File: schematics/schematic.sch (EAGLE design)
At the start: 14 parts, among them U1 TSR_1-2450

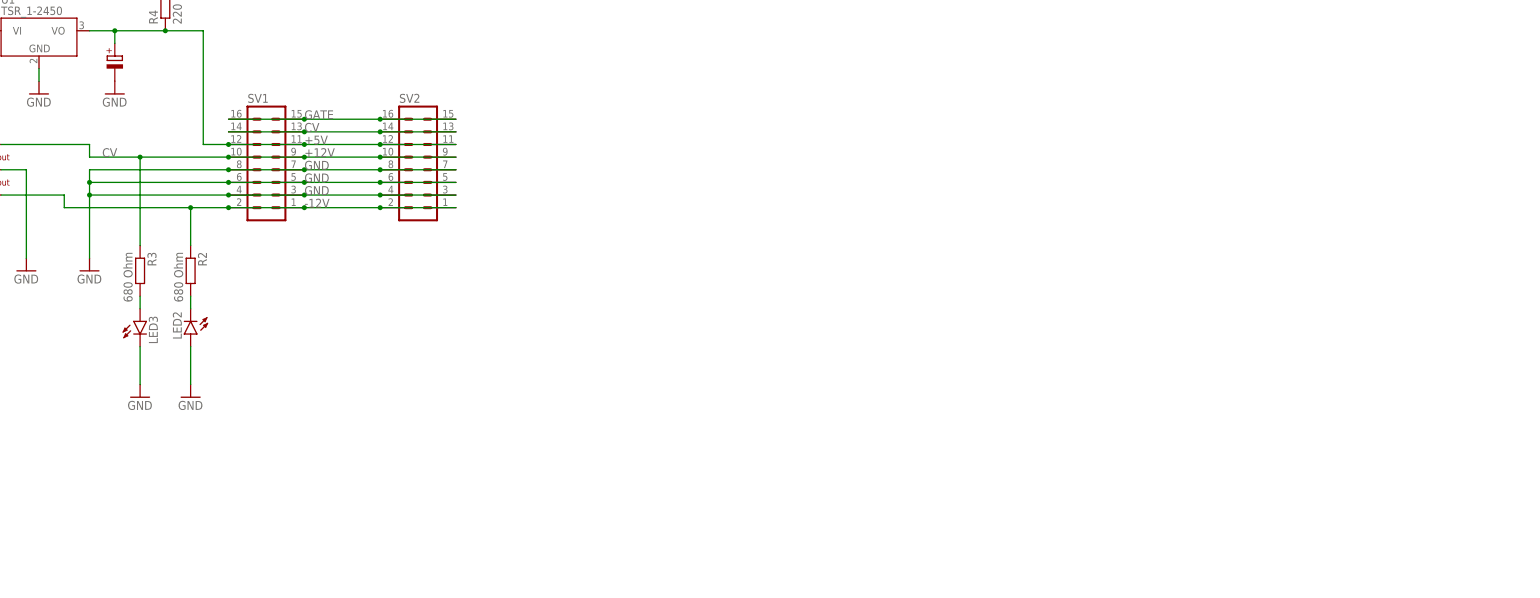
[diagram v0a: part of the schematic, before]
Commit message: changed schematic
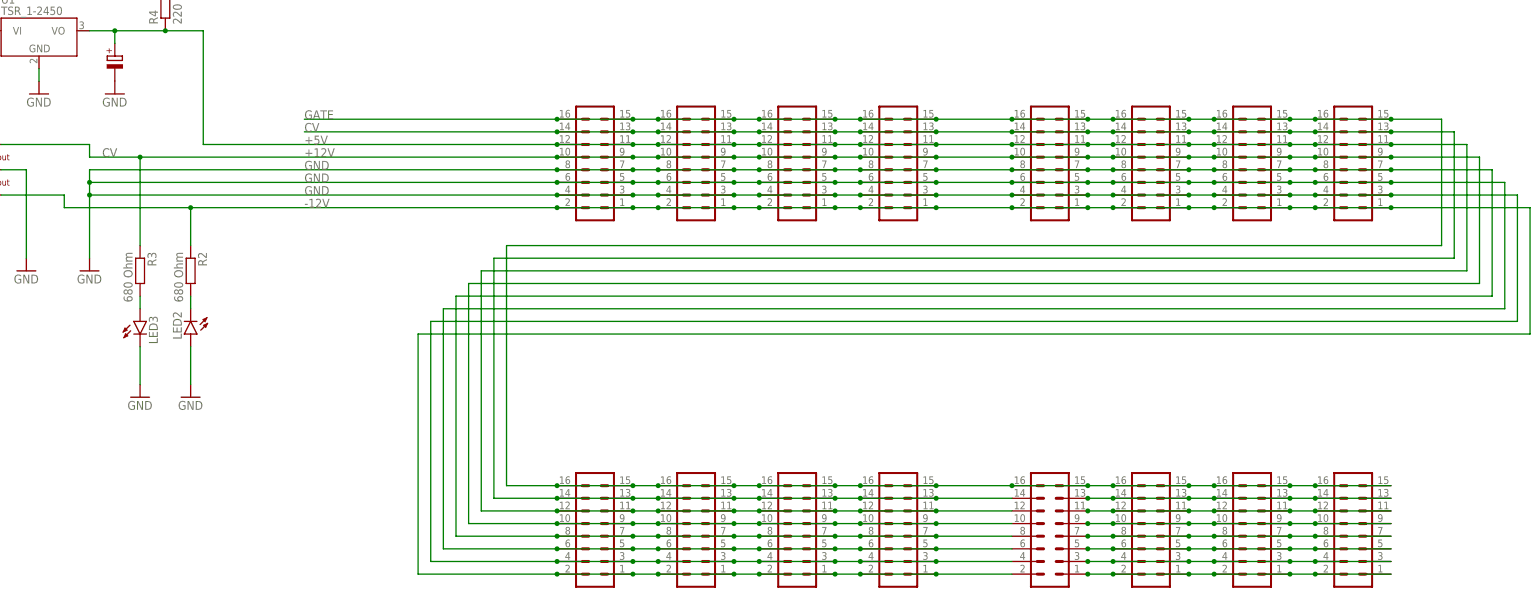
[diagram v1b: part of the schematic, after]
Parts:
- removed SV1: (no value), con-lstb:MA08-2W
- added SV10, SV11, SV12, SV13, SV14, SV15, SV16, SV17, SV3, SV4, SV5, SV6, SV7, SV8, SV9: (no value), con-lstb:MA08-2W
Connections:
- new net N$30: SV14.1, SV15.1, SV15.2, SV16.1, SV16.2, SV17.1, SV17.2
- new net N$31: SV14.3, SV15.3, SV15.4, SV16.3, SV16.4, SV17.3, SV17.4
- new net N$32: SV14.5, SV15.5, SV15.6, SV16.5, SV16.6, SV17.5, SV17.6
- new net N$33: SV14.7, SV15.7, SV15.8, SV16.7, SV16.8, SV17.7, SV17.8
- new net N$34: SV14.9, SV15.10, SV15.9, SV16.10, SV16.9, SV17.10, SV17.9
- new net N$35: SV14.11, SV15.11, SV15.12, SV16.11, SV16.12, SV17.11, SV17.12
- new net N$36: SV14.13, SV15.13, SV15.14, SV16.13, SV16.14, SV17.13, SV17.14
- net +12V: now also SV10.10, SV10.9, SV11.10, SV11.9, SV12.10, SV12.9, SV13.10, SV13.9, SV14.10, SV3.10, SV3.9, SV4.10, SV4.9, SV5.10, SV5.9, SV6.10, SV6.9, SV7.10, SV7.9, SV8.10, SV8.9, SV9.10, SV9.9; no longer SV1.10, SV1.9
- net +5V: now also SV10.11, SV10.12, SV11.11, SV11.12, SV12.11, SV12.12, SV13.11, SV13.12, SV14.12, SV3.11, SV3.12, SV4.11, SV4.12, SV5.11, SV5.12, SV6.11, SV6.12, SV7.11, SV7.12, SV8.11, SV8.12, SV9.11, SV9.12; no longer SV1.11, SV1.12
- net -12V: now also SV10.1, SV10.2, SV11.1, SV11.2, SV12.1, SV12.2, SV13.1, SV13.2, SV14.2, SV3.1, SV3.2, SV4.1, SV4.2, SV5.1, SV5.2, SV6.1, SV6.2, SV7.1, SV7.2, SV8.1, SV8.2, SV9.1, SV9.2; no longer SV1.1, SV1.2
- net CV: now also SV10.13, SV10.14, SV11.13, SV11.14, SV12.13, SV12.14, SV13.13, SV13.14, SV14.14, SV3.13, SV3.14, SV4.13, SV4.14, SV5.13, SV5.14, SV6.13, SV6.14, SV7.13, SV7.14, SV8.13, SV8.14, SV9.13, SV9.14; no longer SV1.13, SV1.14
- net GATE: now also SV10.15, SV10.16, SV11.15, SV11.16, SV12.15, SV12.16, SV13.15, SV13.16, SV14.15, SV14.16, SV15.15, SV15.16, SV16.15, SV16.16, SV17.15, SV17.16, SV3.15, SV3.16, SV4.15, SV4.16, SV5.15, SV5.16, SV6.15, SV6.16, SV7.15, SV7.16, SV8.15, SV8.16, SV9.15, SV9.16; no longer SV1.15, SV1.16
- net GND: now also SV10.3, SV10.4, SV10.5, SV10.6, SV10.7, SV10.8, SV11.3, SV11.4, SV11.5, SV11.6, SV11.7, SV11.8, SV12.3, SV12.4, SV12.5, SV12.6, SV12.7, SV12.8, SV13.3, SV13.4, SV13.5, SV13.6, SV13.7, SV13.8, SV14.4, SV14.6, SV14.8, SV3.3, SV3.4, SV3.5, SV3.6, SV3.7, SV3.8, SV4.3, SV4.4, SV4.5, SV4.6, SV4.7, SV4.8, SV5.3, SV5.4, SV5.5, SV5.6, SV5.7, SV5.8, SV6.3, SV6.4, SV6.5, SV6.6, SV6.7, SV6.8, SV7.3, SV7.4, SV7.5, SV7.6, SV7.7, SV7.8, SV8.3, SV8.4, SV8.5, SV8.6, SV8.7, SV8.8, SV9.3, SV9.4, SV9.5, SV9.6, SV9.7, SV9.8; no longer SV1.3, SV1.4, SV1.5, SV1.6, SV1.7, SV1.8

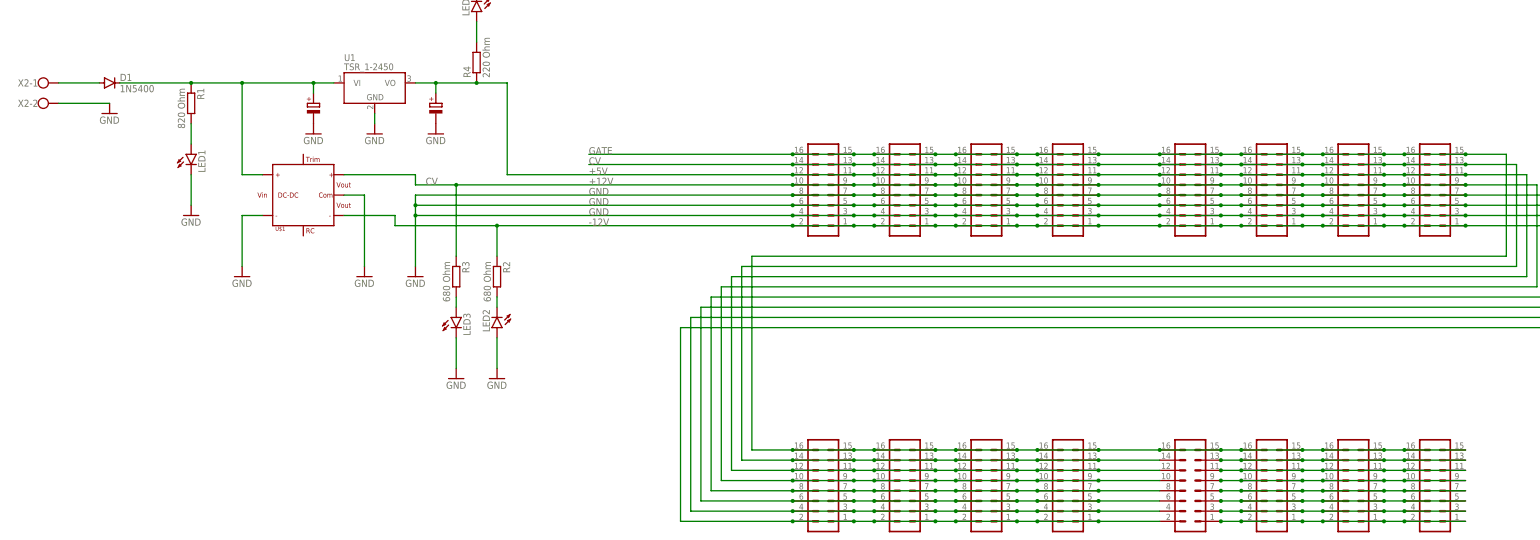
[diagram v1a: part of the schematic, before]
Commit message: fixed power header connections
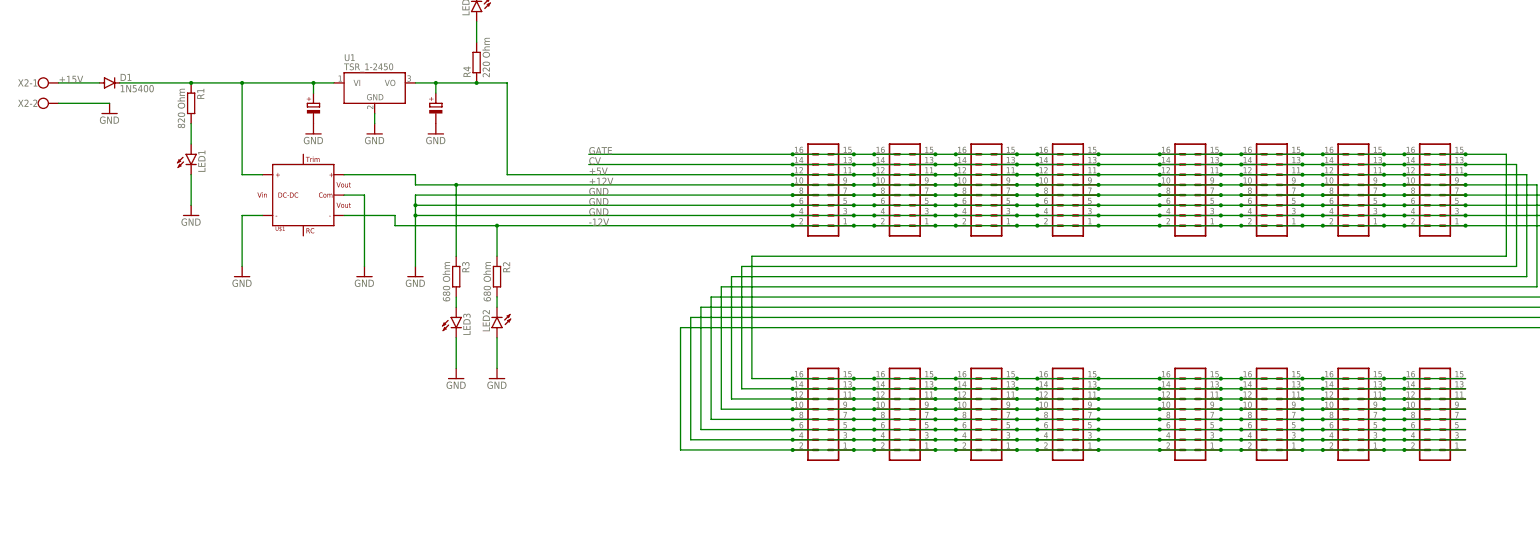
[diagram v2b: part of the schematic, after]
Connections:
- net N$1 renamed +15V
- removed net N$30: SV14.1, SV15.1, SV15.2, SV16.1, SV16.2, SV17.1, SV17.2
- removed net N$31: SV14.3, SV15.3, SV15.4, SV16.3, SV16.4, SV17.3, SV17.4
- removed net N$32: SV14.5, SV15.5, SV15.6, SV16.5, SV16.6, SV17.5, SV17.6
- removed net N$33: SV14.7, SV15.7, SV15.8, SV16.7, SV16.8, SV17.7, SV17.8
- removed net N$34: SV14.9, SV15.10, SV15.9, SV16.10, SV16.9, SV17.10, SV17.9
- removed net N$35: SV14.11, SV15.11, SV15.12, SV16.11, SV16.12, SV17.11, SV17.12
- removed net N$36: SV14.13, SV15.13, SV15.14, SV16.13, SV16.14, SV17.13, SV17.14
- net +12V: now also SV14.9, SV15.10, SV15.9, SV16.10, SV16.9, SV17.10, SV17.9
- net +5V: now also SV14.11, SV15.11, SV15.12, SV16.11, SV16.12, SV17.11, SV17.12
- net -12V: now also SV14.1, SV15.1, SV15.2, SV16.1, SV16.2, SV17.1, SV17.2
- net CV: now also SV14.13, SV15.13, SV15.14, SV16.13, SV16.14, SV17.13, SV17.14
- net GND: now also SV14.3, SV14.5, SV14.7, SV15.3, SV15.4, SV15.5, SV15.6, SV15.7, SV15.8, SV16.3, SV16.4, SV16.5, SV16.6, SV16.7, SV16.8, SV17.3, SV17.4, SV17.5, SV17.6, SV17.7, SV17.8

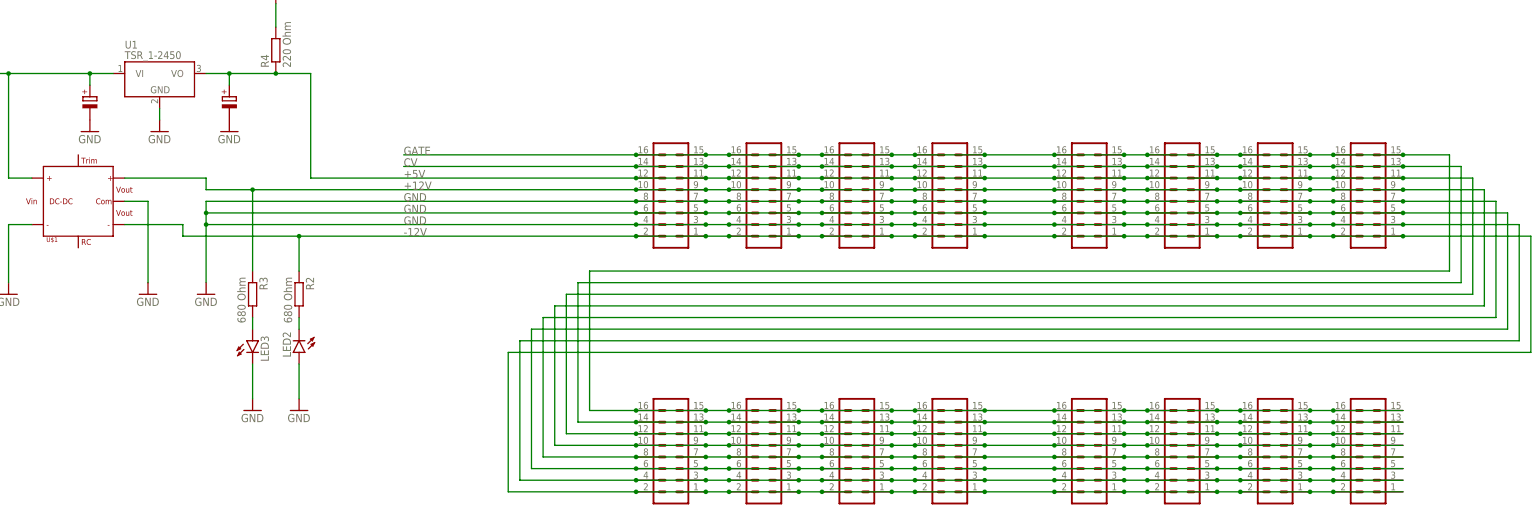
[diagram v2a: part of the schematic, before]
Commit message: added first board layout
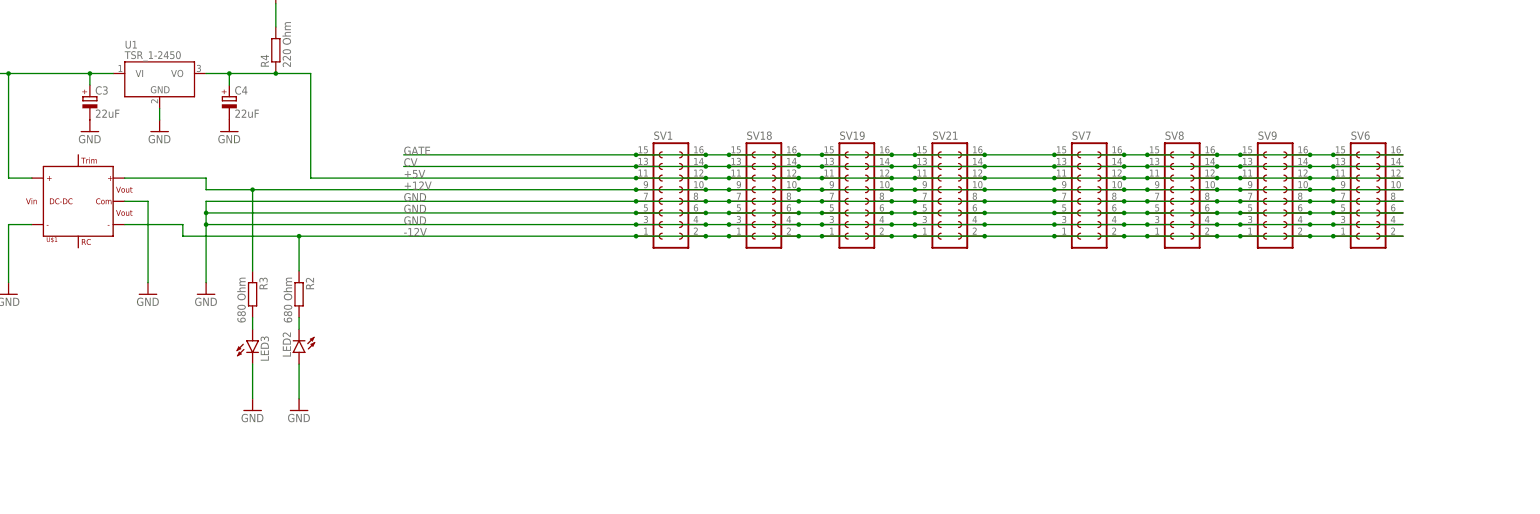
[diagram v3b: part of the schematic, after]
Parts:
- removed SV10, SV11, SV12, SV13, SV14, SV15, SV16, SV17, SV2, SV3, SV4, SV5: (no value), con-lstb:MA08-2W
- added C3, C4: 22uF, rcl:CPOL-EUE2.5-5
- added SV1, SV18, SV19, SV21: (no value), con-lsta:FE08-2
- R1, R2, R3, R4: device rcl:R-EU_0204/7 -> rcl:R-EU_0207/10
- SV6, SV7, SV8, SV9: device con-lstb:MA08-2W -> con-lsta:FE08-2
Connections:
- net +12V: now also SV1.10, SV1.9, SV18.10, SV18.9, SV19.10, SV19.9, SV21.10, SV21.9; no longer SV10.10, SV10.9, SV11.10, SV11.9, SV12.10, SV12.9, SV13.10, SV13.9, SV14.10, SV14.9, SV15.10, SV15.9, SV16.10, SV16.9, SV17.10, SV17.9, SV2.10, SV2.9, SV3.10, SV3.9, SV4.10, SV4.9, SV5.10, SV5.9
- net +5V: now also C4.+, SV1.11, SV1.12, SV18.11, SV18.12, SV19.11, SV19.12, SV21.11, SV21.12; no longer SV10.11, SV10.12, SV11.11, SV11.12, SV12.11, SV12.12, SV13.11, SV13.12, SV14.11, SV14.12, SV15.11, SV15.12, SV16.11, SV16.12, SV17.11, SV17.12, SV2.11, SV2.12, SV3.11, SV3.12, SV4.11, SV4.12, SV5.11, SV5.12
- net -12V: now also SV1.1, SV1.2, SV18.1, SV18.2, SV19.1, SV19.2, SV21.1, SV21.2; no longer SV10.1, SV10.2, SV11.1, SV11.2, SV12.1, SV12.2, SV13.1, SV13.2, SV14.1, SV14.2, SV15.1, SV15.2, SV16.1, SV16.2, SV17.1, SV17.2, SV2.1, SV2.2, SV3.1, SV3.2, SV4.1, SV4.2, SV5.1, SV5.2
- net CV: now also SV1.13, SV1.14, SV18.13, SV18.14, SV19.13, SV19.14, SV21.13, SV21.14; no longer SV10.13, SV10.14, SV11.13, SV11.14, SV12.13, SV12.14, SV13.13, SV13.14, SV14.13, SV14.14, SV15.13, SV15.14, SV16.13, SV16.14, SV17.13, SV17.14, SV2.13, SV2.14, SV3.13, SV3.14, SV4.13, SV4.14, SV5.13, SV5.14
- net GATE: now also SV1.15, SV1.16, SV18.15, SV18.16, SV19.15, SV19.16, SV21.15, SV21.16; no longer SV10.15, SV10.16, SV11.15, SV11.16, SV12.15, SV12.16, SV13.15, SV13.16, SV14.15, SV14.16, SV15.15, SV15.16, SV16.15, SV16.16, SV17.15, SV17.16, SV2.15, SV2.16, SV3.15, SV3.16, SV4.15, SV4.16, SV5.15, SV5.16
- net GND: now also C3.-, C4.-, SV1.3, SV1.4, SV1.5, SV1.6, SV1.7, SV1.8, SV18.3, SV18.4, SV18.5, SV18.6, SV18.7, SV18.8, SV19.3, SV19.4, SV19.5, SV19.6, SV19.7, SV19.8, SV21.3, SV21.4, SV21.5, SV21.6, SV21.7, SV21.8; no longer SV10.3, SV10.4, SV10.5, SV10.6, SV10.7, SV10.8, SV11.3, SV11.4, SV11.5, SV11.6, SV11.7, SV11.8, SV12.3, SV12.4, SV12.5, SV12.6, SV12.7, SV12.8, SV13.3, SV13.4, SV13.5, SV13.6, SV13.7, SV13.8, SV14.3, SV14.4, SV14.5, SV14.6, SV14.7, SV14.8, SV15.3, SV15.4, SV15.5, SV15.6, SV15.7, SV15.8, SV16.3, SV16.4, SV16.5, SV16.6, SV16.7, SV16.8, SV17.3, SV17.4, SV17.5, SV17.6, SV17.7, SV17.8, SV2.3, SV2.4, SV2.5, SV2.6, SV2.7, SV2.8, SV3.3, SV3.4, SV3.5, SV3.6, SV3.7, SV3.8, SV4.3, SV4.4, SV4.5, SV4.6, SV4.7, SV4.8, SV5.3, SV5.4, SV5.5, SV5.6, SV5.7, SV5.8
- net VI: now also C3.+

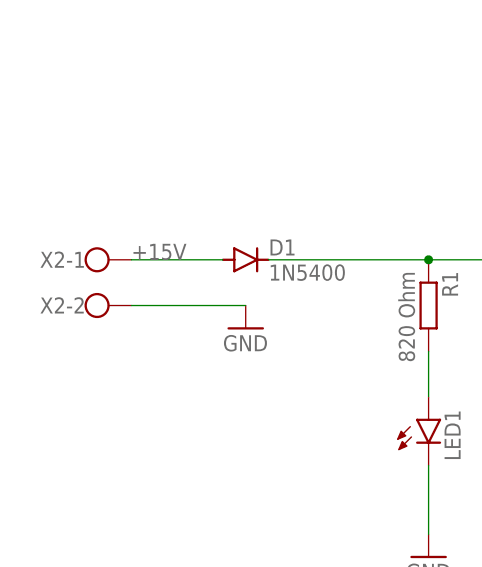
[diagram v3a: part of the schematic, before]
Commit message: added double input screw terminals
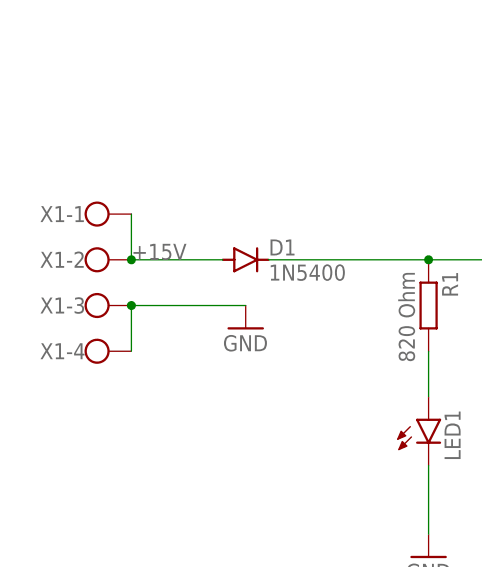
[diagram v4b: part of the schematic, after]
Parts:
- removed X2: (no value), con-wago-500:W237-102
- added X1: (no value), con-wago-500:W237-4
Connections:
- net +15V: now also X1-1.KL, X1-2.KL; no longer X2-1.KL
- net GND: now also X1-3.KL, X1-4.KL; no longer X2-2.KL
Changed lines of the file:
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@@
 <parts>
 <part name="U$1" library="dk30a" deviceset="DKA30" device="&quot;"/>
-<part name="X2" library="con-wago-500" library_urn="urn:adsk.eagle:library:195" deviceset="W237-102" device="" package3d_urn="urn:adsk.eagle:package:10688/1"/>
 <part name="GND1" library="supply1" library_urn="urn:adsk.eagle:library:371" deviceset="GND" device=""/>
 <part name="D1" library="diode" library_urn="urn:adsk.eagle:library:210" deviceset="1N5400" device="" package3d_urn="urn:adsk.eagle:package:43365/2"/>
@@
 <part name="SV8" library="con-lsta" library_urn="urn:adsk.eagle:library:161" deviceset="FE08-2" device="" package3d_urn="urn:adsk.eagle:package:8174/1"/>
 <part name="SV9" library="con-lsta" library_urn="urn:adsk.eagle:library:161" deviceset="FE08-2" device="" package3d_urn="urn:adsk.eagle:package:8174/1"/>
+<part name="X1" library="con-wago-500" library_urn="urn:adsk.eagle:library:195" deviceset="W237-4" device="" package3d_urn="urn:adsk.eagle:package:10695/1"/>
 </parts>
 <sheets>
@@
 <attribute name="NAME" x="59.055" y="59.69" size="1.016" layer="94" font="vector"/>
 </instance>
-<instance part="X2" gate="-1" x="0" y="96.52" smashed="yes">
-<attribute name="NAME" x="0" y="97.409" size="1.778" layer="95" rot="R180"/>
-</instance>
-<instance part="X2" gate="-2" x="0" y="91.44" smashed="yes">
-<attribute name="VALUE" x="-2.54" y="87.757" size="1.778" layer="96"/>
-<attribute name="NAME" x="0" y="92.329" size="1.778" layer="95" rot="R180"/>
-</instance>
 <instance part="GND1" gate="1" x="17.78" y="88.9" smashed="yes">
 <attribute name="VALUE" x="15.24" y="86.36" size="1.778" layer="96"/>
@@
 <attribute name="VALUE" x="323.85" y="55.88" size="1.778" layer="96"/>
 <attribute name="NAME" x="323.85" y="82.042" size="1.778" layer="95"/>
+</instance>
+<instance part="X1" gate="-1" x="0" y="101.6" smashed="yes">
+<attribute name="NAME" x="0" y="102.489" size="1.778" layer="95" rot="R180"/>
+</instance>
+<instance part="X1" gate="-2" x="0" y="96.52" smashed="yes">
+<attribute name="NAME" x="0" y="97.409" size="1.778" layer="95" rot="R180"/>
+</instance>
+<instance part="X1" gate="-3" x="0" y="91.44" smashed="yes">
+<attribute name="NAME" x="0" y="92.329" size="1.778" layer="95" rot="R180"/>
+</instance>
+<instance part="X1" gate="-4" x="0" y="86.36" smashed="yes">
+<attribute name="VALUE" x="-2.54" y="82.677" size="1.778" layer="96"/>
+<attribute name="NAME" x="0" y="87.249" size="1.778" layer="95" rot="R180"/>
 </instance>
 </instances>
@@
 <net name="GND" class="0">
 <segment>
-<pinref part="X2" gate="-2" pin="KL"/>
 <pinref part="GND1" gate="1" pin="GND"/>
 <wire x1="5.08" y1="91.44" x2="17.78" y2="91.44" width="0.1524" layer="91"/>
+<pinref part="X1" gate="-3" pin="KL"/>
+<pinref part="X1" gate="-4" pin="KL"/>
+<wire x1="5.08" y1="91.44" x2="5.08" y2="86.36" width="0.1524" layer="91"/>
+<junction x="5.08" y="91.44"/>
 </segment>
 <segment>
@@
 <net name="+15V" class="0">
 <segment>
-<pinref part="X2" gate="-1" pin="KL"/>
 <pinref part="D1" gate="1" pin="A"/>
 <wire x1="5.08" y1="96.52" x2="15.24" y2="96.52" width="0.1524" layer="91"/>
 <label x="5.08" y="96.52" size="1.778" layer="95"/>
+<pinref part="X1" gate="-2" pin="KL"/>
+<pinref part="X1" gate="-1" pin="KL"/>
+<wire x1="5.08" y1="101.6" x2="5.08" y2="96.52" width="0.1524" layer="91"/>
+<junction x="5.08" y="96.52"/>
 </segment>
 </net>
